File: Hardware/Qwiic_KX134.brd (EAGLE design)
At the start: 25.4 x 25.4 mm, 52 parts, among them J2 QWIIC_RIGHT_ANGLE, J4 QWIIC_RIGHT_ANGLE, U1 KX134

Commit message: adding axes
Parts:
- added U$28: (no value), output:X0
- added U$29: (no value), output:Y0
- added U$30: (no value), output:Z0
- moved U$16 21.9 mm to (2.67, 7.75)
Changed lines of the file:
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@@
 <layer number="24" name="bOrigins" color="15" fill="1" visible="yes" active="yes"/>
 <layer number="25" name="tNames" color="7" fill="1" visible="no" active="yes"/>
-<layer number="26" name="bNames" color="7" fill="1" visible="yes" active="yes"/>
+<layer number="26" name="bNames" color="7" fill="1" visible="no" active="yes"/>
 <layer number="27" name="tValues" color="7" fill="1" visible="no" active="yes"/>
 <layer number="28" name="bValues" color="7" fill="1" visible="yes" active="yes"/>
@@
 <text x="12.7" y="35.56" size="1.778" layer="47" font="vector" ratio="15" align="center">Dimensions in inches</text>
 <text x="13.97" y="-7.62" size="1.778" layer="51" font="vector" ratio="10">Andy England</text>
+<wire x1="19.05" y1="17.78" x2="19.431" y2="18.161" width="0.2032" layer="21"/>
+<wire x1="19.05" y1="17.78" x2="19.431" y2="17.399" width="0.2032" layer="21"/>
+<wire x1="20.32" y1="18.288" x2="20.32" y2="19.05" width="0.2032" layer="21"/>
+<wire x1="20.32" y1="19.05" x2="20.701" y2="18.669" width="0.2032" layer="21"/>
+<wire x1="20.32" y1="19.05" x2="19.939" y2="18.669" width="0.2032" layer="21"/>
+<circle x="20.32" y="17.78" radius="0.457903125" width="0.2032" layer="21"/>
+<circle x="20.32" y="17.78" radius="0.0762" width="0.2032" layer="21"/>
+<wire x1="19.05" y1="17.78" x2="19.812" y2="17.78" width="0.2032" layer="21"/>
 </plain>
 <attributes>
@@
 </element>
 <element name="U$15" library="SparkFun-Buzzard" package="I2C" value="" x="14.605" y="15.875" smashed="yes" rot="MR0"/>
-<element name="U$16" library="SparkFun-Aesthetics" package="QWIIC_5MM" value="" x="22.352" y="17.399" smashed="yes"/>
+<element name="U$16" library="SparkFun-Aesthetics" package="QWIIC_5MM" value="" x="2.667" y="7.747" smashed="yes"/>
 <element name="U$17" library="SparkFun-Buzzard" package="PWR_TO" value="" x="3.81" y="19.812" smashed="yes"/>
 <element name="U1" library="KX134" package="KX134" value="KX134" x="12.7" y="12.7" smashed="yes">
@@
 <element name="U$26" library="output" package="#SDO#0" value="" x="12.7" y="1.778" smashed="yes" rot="MR90"/>
 <element name="U$27" library="output" package="KX134_ACCELEROMETER0" value="" x="21.59" y="12.7" smashed="yes" rot="MR0"/>
+<element name="U$28" library="output" package="X0" value="" x="19.304" y="19.685" smashed="yes"/>
+<element name="U$29" library="output" package="Y0" value="" x="17.399" y="18.034" smashed="yes"/>
+<element name="U$30" library="output" package="Z0" value="" x="20.32" y="17.907" smashed="yes"/>
 </elements>
 <signals>

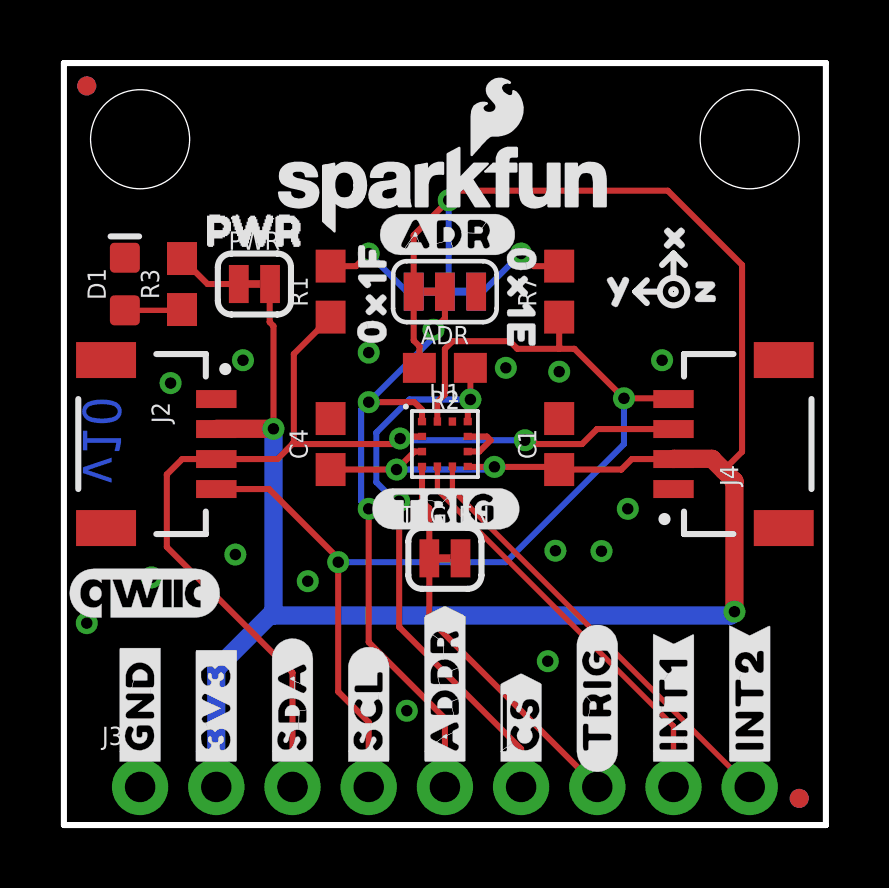
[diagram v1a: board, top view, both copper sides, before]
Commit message: Post review/checklist changes
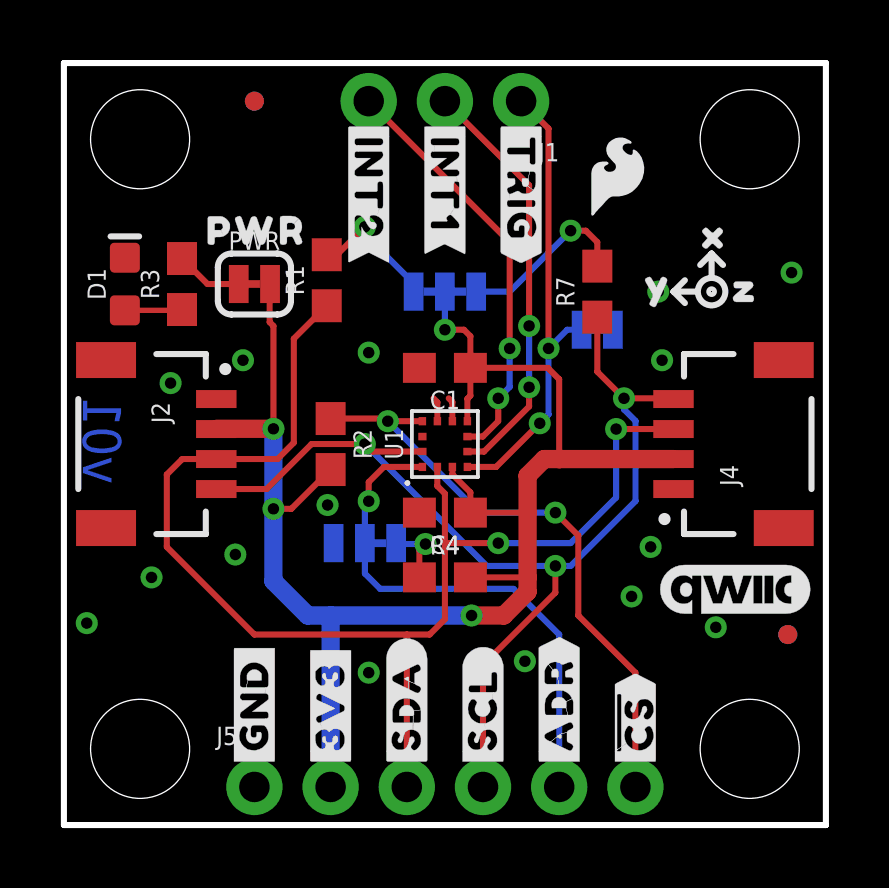
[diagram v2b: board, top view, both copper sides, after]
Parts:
- removed J3: (no value), SparkFun-Connectors:1X09_NO_SILK
- removed LOGO3, LOGO4: SFE_LOGO_NAME_FLAME.1_INCH, SparkFun-Aesthetics:SFE_LOGO_NAME_FLAME_.1
- removed TRG_EN: JUMPER-SMT_2_NC_TRACE_SILK, SparkFun-Jumpers:SMT-JUMPER_2_NC_TRACE_SILK
- added J1: (no value), SparkFun-Connectors:1X03_NO_SILK
- added J5: (no value), SparkFun-Connectors:1X06_NO_SILK
- added JP7, JP8: STAND-OFF, SparkFun:STAND-OFF
- added LOGO1, LOGO2: SFE_LOGO_FLAME.1_INCH, SparkFun-Aesthetics:SFE_LOGO_FLAME_.1
- added R4: 4.7k, SparkFun-Resistors:0603
- added TRIG: JUMPER-SMT_2_NC_TRACE_SILK, SparkFun-Jumpers:SMT-JUMPER_2_NC_TRACE_SILK
- added U$31: (no value), output:PWR0
- added U$32: (no value), output:Z0
- J2, J4: value QWIIC_RIGHT_ANGLE -> QWIIC
- U$1: device output:#ADDR#0 -> output:X0
- U$10: device output:#TRIG#0 -> output:#ADR#0
- U$15: device SparkFun-Buzzard:I2C -> output:#TRIG#0
- U$17: device SparkFun-Buzzard:PWR_TO -> output:#TRIG#2
- U$20: device output:#ADR#0 -> output:#ADR#3
- U$21: device output:#TRIG#0 -> output:Y0
- moved U$18 25.3 mm to (10.2, 23.6), turned to 270 degrees
- moved U$19 25.3 mm to (10.2, 23.6), turned to 270 degrees
- moved U$12 23.1 mm to (12.7, 23.6), turned to 270 degrees
- moved U$13 23.1 mm to (12.7, 23.6), turned to 270 degrees
- moved U$11 22.0 mm to (15.2, 23.6), flipped to the top, turned to 270 degrees
- moved U$1 20.5 mm to (22.7, 19.7), flipped to the bottom, turned to 0 degrees
- moved U$16 19.7 mm to (22.4, 7.87)
- moved U$20 18.9 mm to (16.5, 1.78), turned to 90 degrees
- moved U$17 17.2 mm to (20.2, 14.6), flipped to the bottom
- moved U$14 14.9 mm to (7.49, 7.24), flipped to the bottom, turned to 90 degrees
- moved U$21 12.8 mm to (20.7, 18.0), flipped to the bottom
- moved ADR 8.80 mm to (10.0, 9.40), flipped to the bottom
- moved U$23 8.44 mm to (12.6, 7.24), flipped to the bottom
- moved U$10 7.90 mm to (12.3, 7.49), flipped to the bottom, turned to 0 degrees
- moved U$15 7.77 mm to (15.2, 23.6), turned to 270 degrees
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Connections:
- removed net ADDR/SDO: ADR.2, J3.5, U1.1
- new net ADR/SDO: ADR.2, J5.5, U1.1
- new net N$5: ADR.3, R4.1
- net !CS: now also J5.6; no longer J3.6
- net 3.3V: now also J5.2, R4.2; no longer ADR.3, J3.2
- net GND: now also J5.1, TRIG.2; no longer J3.1, TRG_EN.2
- net INT1: now also J1.2; no longer J3.8
- net INT2: now also J1.3; no longer J3.9
- net SCL/SCLK: now also J5.4; no longer J3.4
- net SDA/SDI: now also J5.3; no longer J3.3
- net TRIG: now also J1.1, TRIG.1; no longer J3.7, TRG_EN.1
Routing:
- net 3.3V: track 82.8 -> 54.7 mm, vias 5 -> 4
- net ADDR/SDO: track 21.1 -> 0.00 mm, vias 3 -> 0
- net ADR/SDO: track 0.00 -> 17.5 mm, vias 0 -> 1
- net SDA/SDI: track 35.4 -> 43.6 mm
- net TRIG: track 13.1 -> 15.6 mm, vias 0 -> 2
- net N$4: track 3.47 -> 5.84 mm
- net N$5: track 0.00 -> 2.19 mm, vias 0 -> 1
- net SCL/SCLK: track 37.9 -> 35.9 mm, vias 2 -> 3
- net N$2: track 3.47 -> 4.49 mm
- net !CS: track 19.3 -> 20.2 mm
- net INT2: track 14.8 -> 14.0 mm, vias 0 -> 2
- net INT1: track 13.9 -> 14.0 mm, vias 0 -> 2
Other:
- board text added: "v01"
- board text removed: "v10"

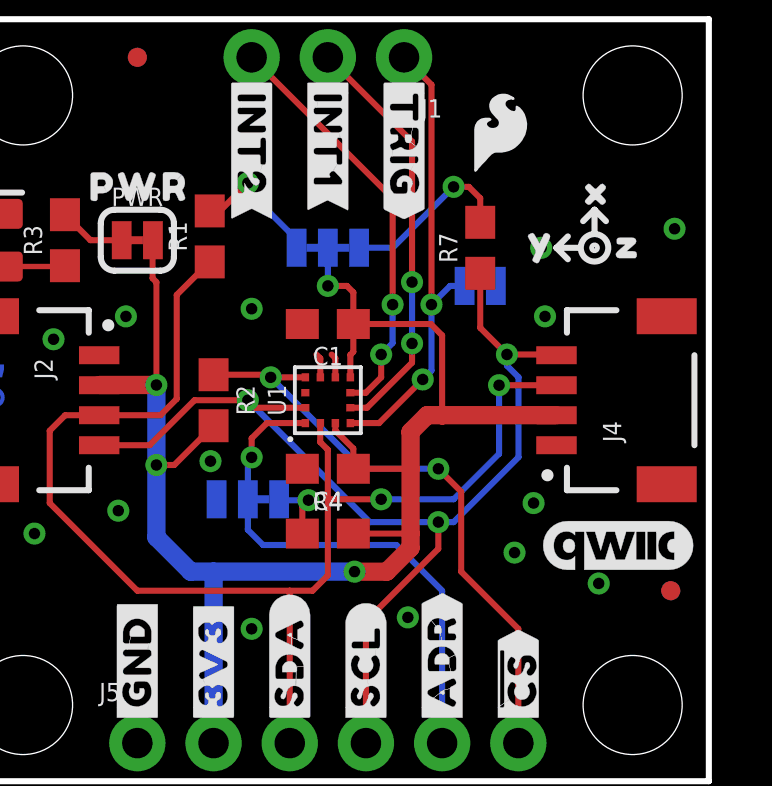
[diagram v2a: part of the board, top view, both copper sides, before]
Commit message: adding 132/134 checkboxes
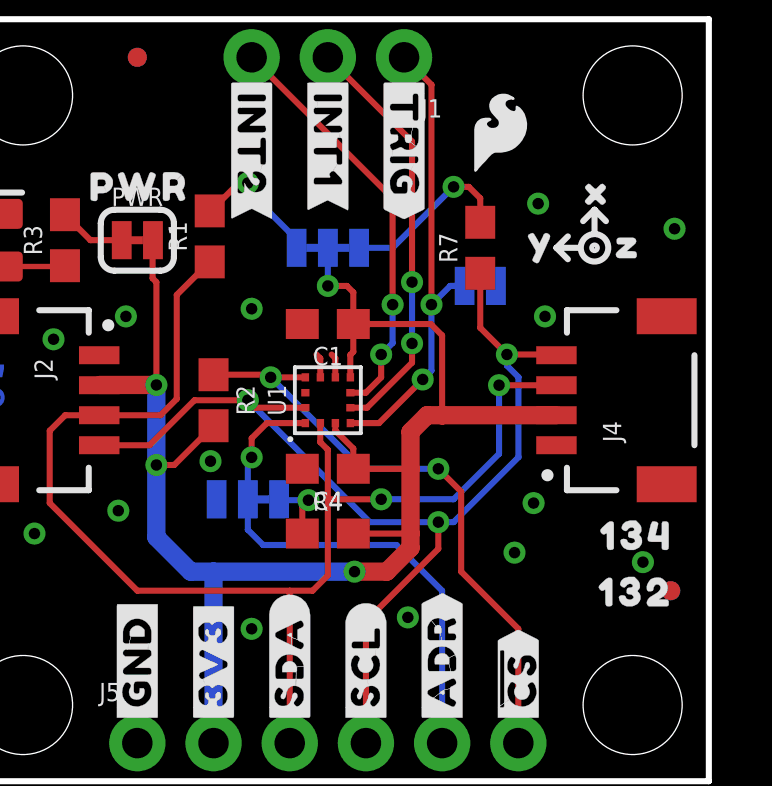
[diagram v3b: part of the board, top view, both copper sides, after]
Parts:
- removed U$16: (no value), SparkFun-Aesthetics:QWIIC_5MM
- added U$33: (no value), output:1320
- added U$34: (no value), output:1340
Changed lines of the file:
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@@
 <wire x1="21.2725" y1="18.0975" x2="21.9075" y2="17.4625" width="0.2032" layer="22"/>
 <wire x1="21.9075" y1="18.0975" x2="21.2725" y2="17.4625" width="0.2032" layer="22"/>
+<rectangle x1="20.5105" y1="7.62" x2="21.59" y2="8.6995" layer="29"/>
+<rectangle x1="20.5105" y1="5.7785" x2="21.59" y2="6.858" layer="29"/>
+<rectangle x1="20.5105" y1="5.7785" x2="21.59" y2="6.858" layer="31"/>
 </plain>
 <attributes>
@@
 <attribute name="VALUE" x="12.7" y="16.637" size="0.6096" layer="28" font="vector" ratio="20" rot="MR0" align="top-center"/>
 </element>
-<element name="U$16" library="SparkFun-Aesthetics" package="QWIIC_5MM" value="" x="22.352" y="7.874" smashed="yes"/>
 <element name="TRIG" library="SparkFun-Jumpers" package="SMT-JUMPER_2_NC_TRACE_SILK" package3d_urn="urn:adsk.eagle:package:39281/1" value="JUMPER-SMT_2_NC_TRACE_SILK" x="17.78" y="16.51" smashed="yes" rot="MR180">
 <attribute name="NAME" x="17.78" y="15.367" size="0.6096" layer="26" font="vector" ratio="20" rot="MR180" align="bottom-center"/>
@@
 <element name="LOGO1" library="SparkFun-Aesthetics" package="SFE_LOGO_FLAME_.1" value="SFE_LOGO_FLAME.1_INCH" x="18.4404" y="21.6408" smashed="yes"/>
 <element name="LOGO2" library="SparkFun-Aesthetics" package="SFE_LOGO_FLAME_.1" value="SFE_LOGO_FLAME.1_INCH" x="18.3896" y="21.59" smashed="yes" rot="MR0"/>
+<element name="U$33" library="output" package="1320" value="" x="21.0312" y="6.2992" smashed="yes"/>
+<element name="U$34" library="output" package="1340" value="" x="21.082" y="8.1788" smashed="yes"/>
 </elements>
 <signals>
@@
 <contactref element="D1" pad="C"/>
 <via x="10.16" y="15.748" extent="1-16" drill="0.381"/>
-<via x="21.7297" y="6.5913" extent="1-16" drill="0.381"/>
+<via x="23.2029" y="7.3025" extent="1-16" drill="0.381"/>
 <via x="3.556" y="14.732" extent="1-16" drill="0.381"/>
 <via x="5.969" y="15.494" extent="1-16" drill="0.381"/>
@@
 <via x="5.715" y="9.017" extent="1-16" drill="0.381"/>
 <via x="0.762" y="6.731" extent="1-16" drill="0.381"/>
-<via x="19.812" y="17.78" extent="1-16" drill="0.381"/>
+<via x="19.7104" y="19.2532" extent="1-16" drill="0.381"/>
 <contactref element="TRIG" pad="2"/>
 <contactref element="C1" pad="2"/>
@@
 <wire x1="10.033" y1="19.685" x2="10.033" y2="19.939" width="0.2032" layer="16"/>
 <via x="10.033" y="19.939" extent="1-16" drill="0.381"/>
-<wire x1="10.033" y1="19.939" x2="9.105" y2="19.011" width="0.2032" layer="1"/>
-<wire x1="8.763" y1="19.011" x2="9.105" y2="19.011" width="0.2032" layer="1"/>
+<wire x1="10.033" y1="19.939" x2="9.7282" y2="19.939" width="0.2032" layer="1"/>
+<wire x1="9.7282" y1="19.939" x2="8.8002" y2="19.011" width="0.2032" layer="1"/>
+<wire x1="8.763" y1="19.011" x2="8.8002" y2="19.011" width="0.2032" layer="1"/>
 </signal>
 <signal name="N$4">
